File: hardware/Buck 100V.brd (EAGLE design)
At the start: 22.5 x 55.2 mm, 31 parts, among them M1 SI3430DV, M2 SI5435BDC, Q1 FMMT625, Q2 FMMT723, U1 LT3756EMSE

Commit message: Add DRC and CAM scripts, some modification to go with new DRC.
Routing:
- net GND: track 27.8 -> 34.4 mm, vias 17 -> 16
- net ISN: track 74.6 -> 70.8 mm
- net CTRL: track 42.3 -> 44.9 mm

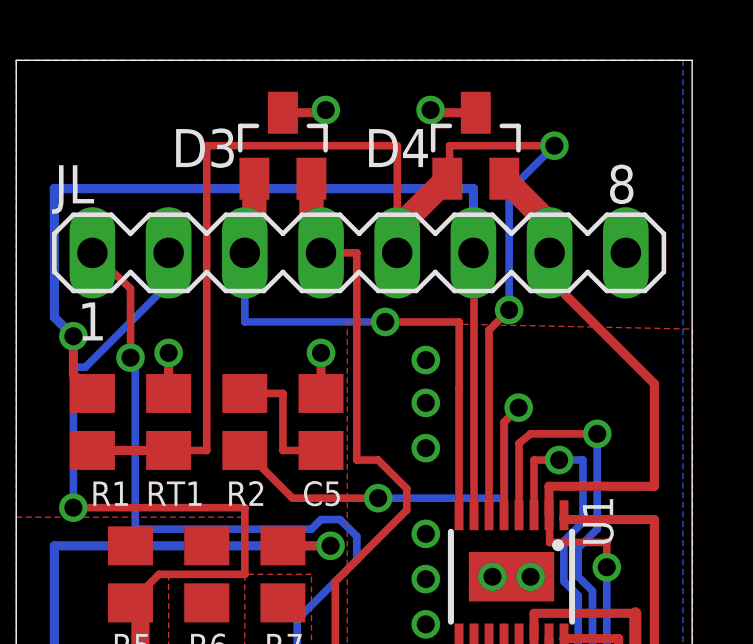
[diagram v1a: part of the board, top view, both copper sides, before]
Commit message: Better routing for ESD protection. Fix airwires.
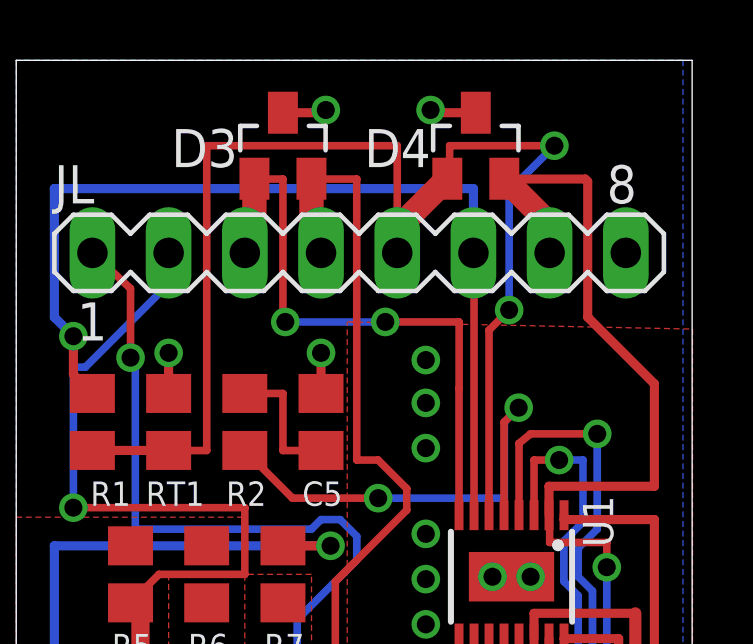
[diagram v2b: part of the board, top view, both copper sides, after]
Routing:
- net FB: track 44.9 -> 49.6 mm
- net /OPEN_LED: track 24.9 -> 27.8 mm
- net PWM: track 18.5 -> 20.7 mm, vias 1 -> 2
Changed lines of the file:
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@@
 <?xml version="1.0" encoding="utf-8"?>
 <!DOCTYPE eagle SYSTEM "eagle.dtd">
-<eagle version="6.2">
+<eagle version="6.1">
 <drawing>
 <settings>
@@
 <wire x1="13.0175" y1="40.9575" x2="12.065" y2="41.91" width="0.254" layer="1"/>
 <wire x1="12.065" y1="41.91" x2="11.350625" y2="41.91" width="0.254" layer="1"/>
-<wire x1="11.350625" y1="41.91" x2="11.350625" y2="48.815625" width="0.254" layer="1"/>
-<wire x1="11.350625" y1="48.815625" x2="10.16" y2="48.815625" width="0.254" layer="1"/>
+<wire x1="11.350625" y1="41.91" x2="11.350625" y2="51.27625" width="0.254" layer="1"/>
+<wire x1="11.350625" y1="51.27625" x2="9.921875" y2="51.27625" width="0.254" layer="1"/>
+<wire x1="9.921875" y1="51.27625" x2="9.921875" y2="51.196875" width="0.254" layer="1"/>
+<wire x1="9.921875" y1="51.27625" x2="9.84" y2="51.27625" width="0.254" layer="1"/>
+<wire x1="9.84" y1="51.27625" x2="9.84" y2="51.2875" width="0.254" layer="1"/>
 </signal>
 <signal name="PWM">
@@
 <wire x1="14.76375" y1="46.51375" x2="12.303125" y2="46.51375" width="0.254" layer="1"/>
 <via x="12.303125" y="46.51375" extent="1-16" drill="0.6"/>
-<wire x1="12.303125" y1="46.51375" x2="7.62" y2="46.51375" width="0.254" layer="16"/>
-<wire x1="7.62" y1="46.51375" x2="7.62" y2="48.815625" width="0.254" layer="16"/>
+<wire x1="12.303125" y1="46.51375" x2="8.969375" y2="46.51375" width="0.254" layer="16"/>
+<via x="8.969375" y="46.51375" extent="1-16" drill="0.6"/>
+<wire x1="8.969375" y1="46.51375" x2="8.89" y2="46.51375" width="0.254" layer="1"/>
+<wire x1="8.89" y1="46.51375" x2="8.89" y2="51.27625" width="0.254" layer="1"/>
+<wire x1="8.89" y1="51.27625" x2="7.94" y2="51.27625" width="0.254" layer="1"/>
+<wire x1="7.94" y1="51.27625" x2="7.94" y2="51.2875" width="0.254" layer="1"/>
 </signal>
 <signal name="N$1">
@@
 <wire x1="5.1054" y1="32.004" x2="8.824" y2="32.004" width="0.6096" layer="1"/>
 <wire x1="8.824" y1="32.004" x2="8.89" y2="32.07" width="0.6096" layer="1"/>
-<wire x1="17.78" y1="48.815625" x2="17.78" y2="47.9425" width="0.3048" layer="1"/>
-<wire x1="17.78" y1="47.9425" x2="21.2725" y2="44.45" width="0.3048" layer="1"/>
 <wire x1="21.2725" y1="44.45" x2="21.2725" y2="41.036875" width="0.3048" layer="1"/>
 <wire x1="21.2725" y1="41.036875" x2="17.76" y2="41.036875" width="0.3048" layer="1"/>
@@
 <wire x1="19.685" y1="39.163625" x2="17.78" y2="39.163625" width="0.254" layer="1"/>
 <wire x1="17.78" y1="40.070625" x2="17.78" y2="39.163625" width="0.254" layer="1"/>
+<wire x1="21.2725" y1="44.45" x2="19.05" y2="46.6725" width="0.3048" layer="1"/>
+<wire x1="19.05" y1="46.6725" x2="19.05" y2="51.196875" width="0.3048" layer="1"/>
+<wire x1="19.05" y1="51.196875" x2="18.970625" y2="51.27625" width="0.3048" layer="1"/>
+<wire x1="18.970625" y1="51.27625" x2="16.271875" y2="51.27625" width="0.3048" layer="1"/>
+<wire x1="16.269375" y1="51.2875" x2="16.271875" y2="51.285" width="0.3048" layer="1"/>
+<wire x1="16.271875" y1="51.285" x2="16.271875" y2="51.27625" width="0.3048" layer="1"/>
 <wire x1="17.78" y1="40.070625" x2="17.76" y2="40.070625" width="0" layer="19" extent="1-1"/>
 </signal>
@@
 </signal>
 </signals>
-<errors>
-</errors>
 </board>
 </drawing>
